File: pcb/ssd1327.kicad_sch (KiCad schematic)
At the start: 7 parts, among them J5 Display Connector Input, J6 Display Connector Output, J7 SSD1327 16-Pin Connector

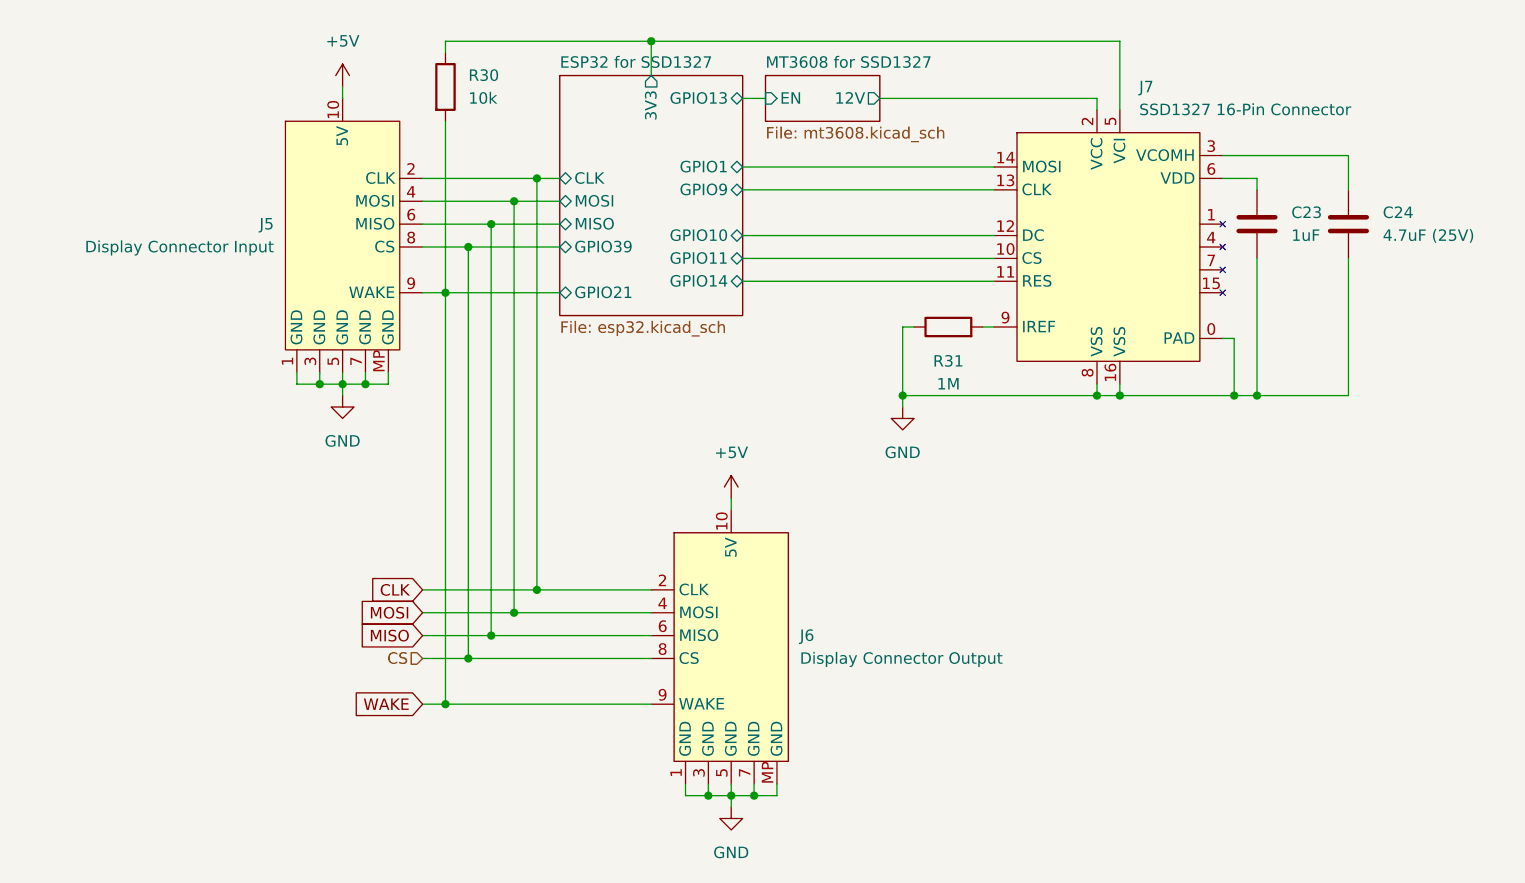
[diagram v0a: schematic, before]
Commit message: Split PCB into modules
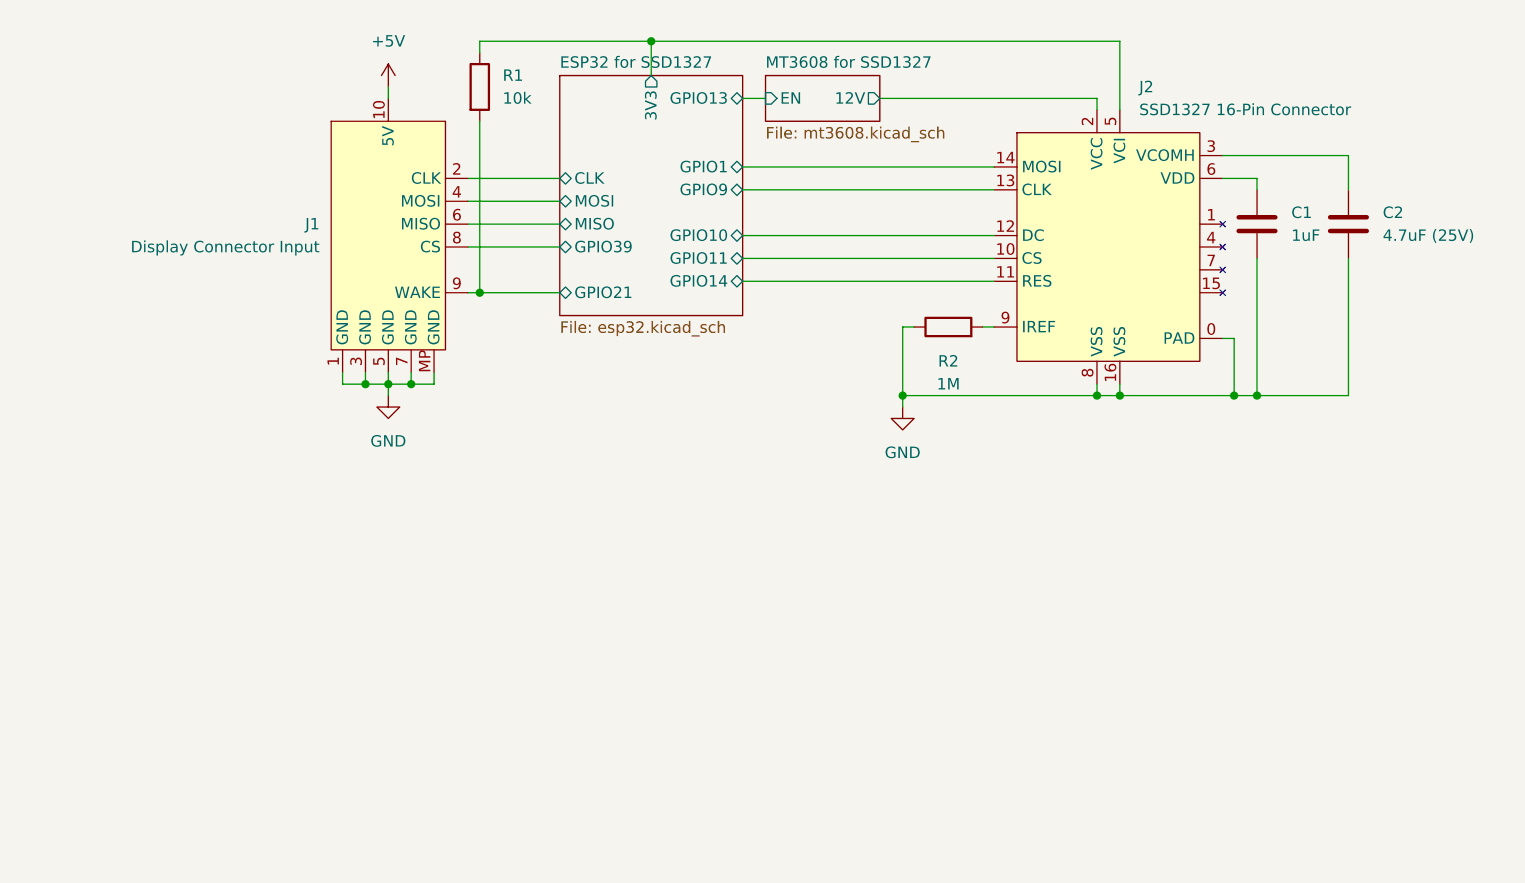
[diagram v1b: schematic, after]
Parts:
- removed J6: Display Connector Output, Connector_Molex:Molex_PicoBlade_53261-1071_1x10-1MP_P1.25mm_Horizontal, symbol Data Connector:Display_Connector_Output
- renumbered C23 to C1, C24 to C2, J5 to J1, J7 to J2, R30 to R1, R31 to R2
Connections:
- net CLK renamed ESP32 for SSD1327/CLK
- net CS renamed ESP32 for SSD1327/GPIO39
- net MISO renamed ESP32 for SSD1327/MISO
- net MOSI renamed ESP32 for SSD1327/MOSI
- net WAKE renamed ESP32 for SSD1327/GPIO21
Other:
- moved on the sheet: J1, R1

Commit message: SSD1327 PCB routing
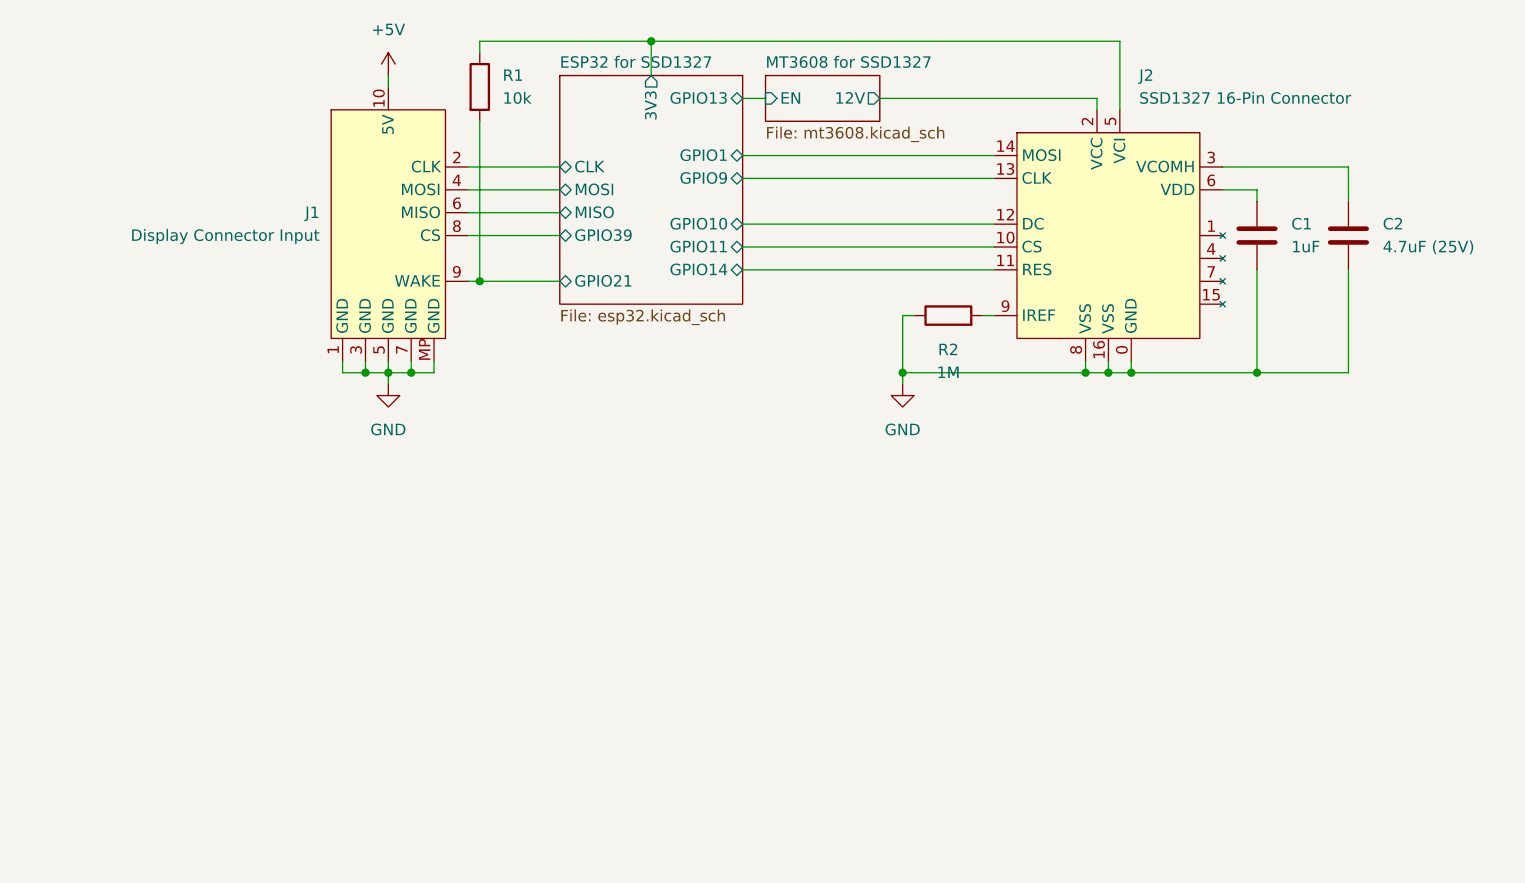
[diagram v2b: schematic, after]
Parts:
- J2: footprint Connector_FFC-FPC:TE_1-1734839-6_1x16-1MP_P0.5mm_Horizontal -> Display_FPC:ssd1327
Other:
- moved on the sheet: C1, C2, J1, J2, R2

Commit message: Master board PCB routing
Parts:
- C2: value 4.7uF (25V) -> 4.7uF
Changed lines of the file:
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@@
 			)
 		)
-		(property "Value" "4.7uF (25V)"
+		(property "Value" "4.7uF"
 			(at 167.64 57.1499 0)
 			(effects
